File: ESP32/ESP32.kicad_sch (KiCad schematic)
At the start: 10 parts, among them U1 TPS63001

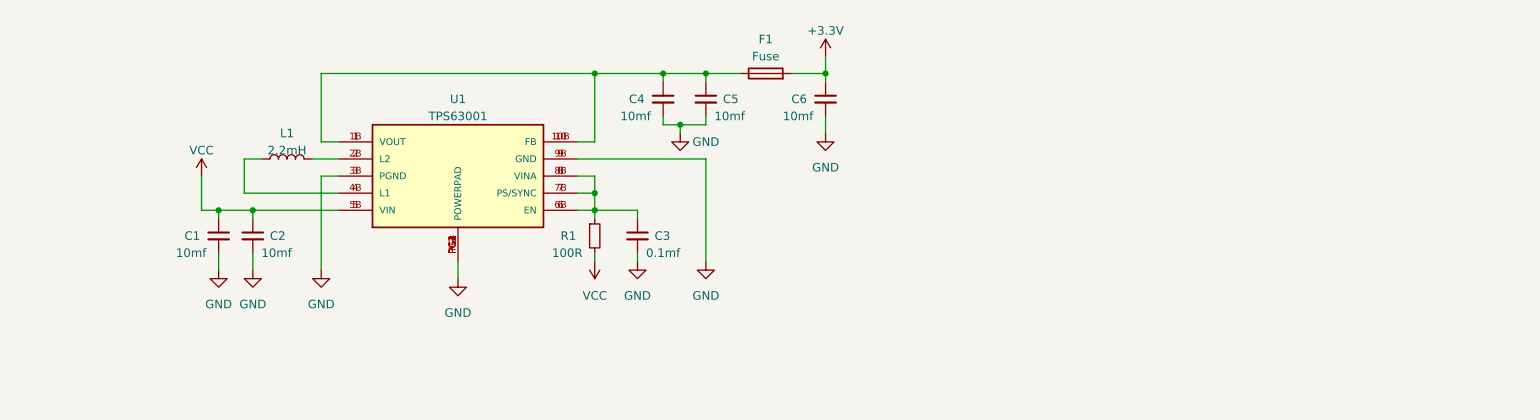
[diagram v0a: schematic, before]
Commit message: added power regulator and battery charger
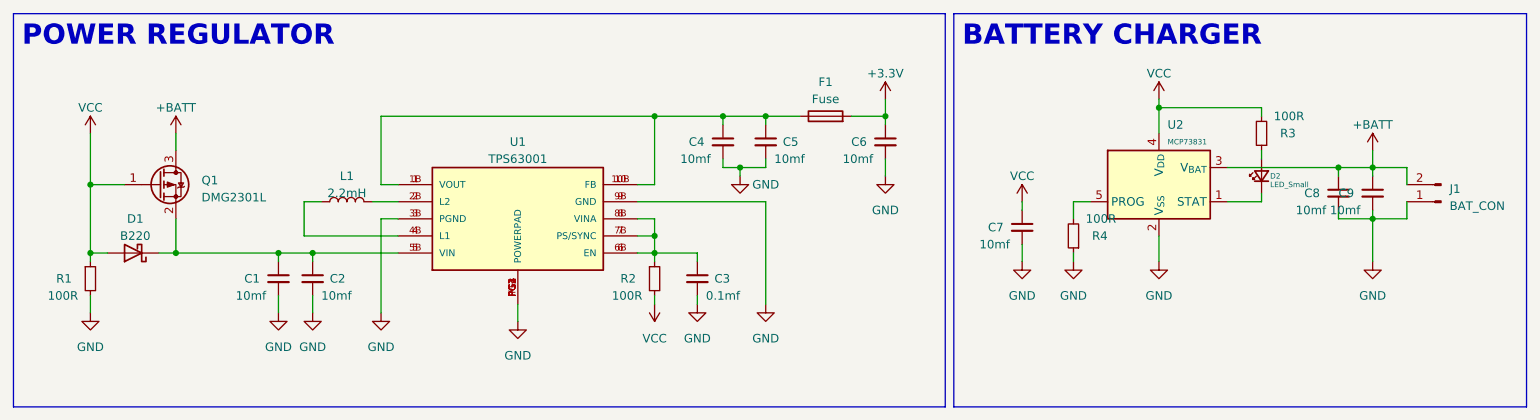
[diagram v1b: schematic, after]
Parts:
- added C7, C8, C9: 10mf, symbol Device:C_Small
- added D1: B220, Diode_SMD:D_SMB, symbol Diode:B220
- added D2: LED_Small, symbol Device:LED_Small
- added J1: BAT_CON, symbol Connector:Conn_01x02_Pin
- added Q1: DMG2301L, Package_TO_SOT_SMD:SOT-23, symbol Transistor_FET:DMG2301L
- added R1, R3, R4: 100R, symbol Device:R_Small
- added U2: MCP73831, Package_TO_SOT_SMD:SOT-23-5, symbol Battery_Management:MCP73831-4-OT
- renumbered R1 to R2
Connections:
- net GND: now also C7.2, C8.2, C9.2, J1.1 (Pin_1), R1.2, R4.1, U2.2 (V_{SS})
- net VCC: now also C7.1, D1.2 (A), Q1.1 (G), R1.1, R3.2, U2.4 (V_{DD}); no longer C1.1, C2.1, U1.5 (VIN), U1.5B (VIN)
- new net: C1.1, C2.1, D1.1 (K), Q1.2 (S), U1.5 (VIN), U1.5B (VIN)
- new net: D2.2 (A), R3.1
- new net: D2.1 (K), U2.1 (STAT)
- new net: R4.2, U2.5 (PROG)
- new net +BATT: C8.1, C9.1, J1.2 (Pin_2), Q1.3 (D), U2.3 (V_{BAT})
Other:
- note added: "BATTERY CHARGER"
- note added: "POWER REGULATOR"
- moved on the sheet: C1, C2, C3, C4, C5, C6, F1, L1, R2, U1

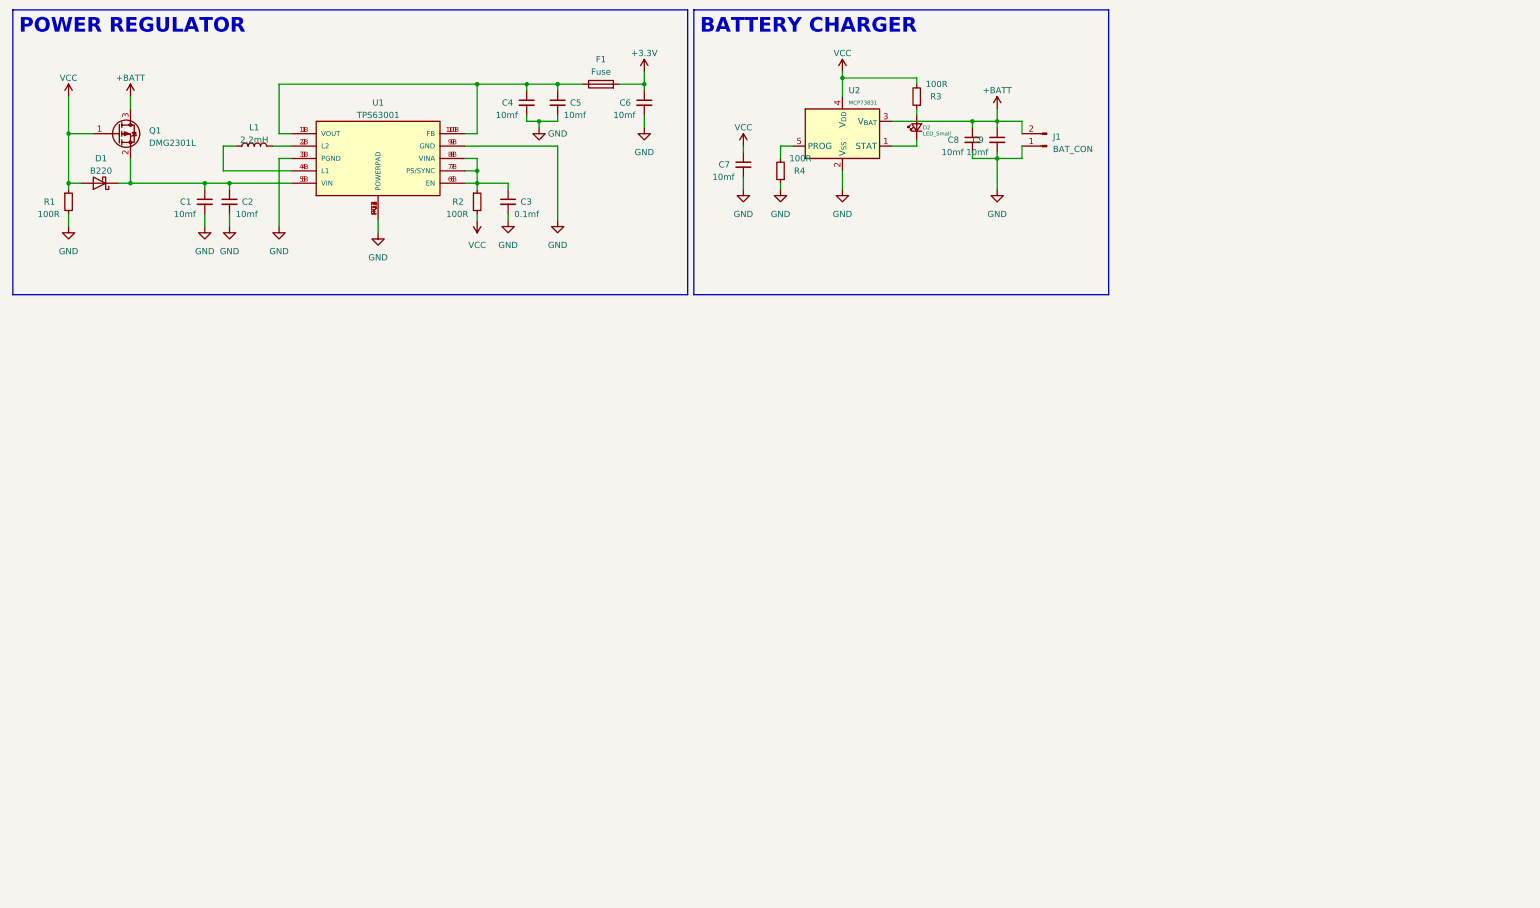
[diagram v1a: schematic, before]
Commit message: addes the memory chips
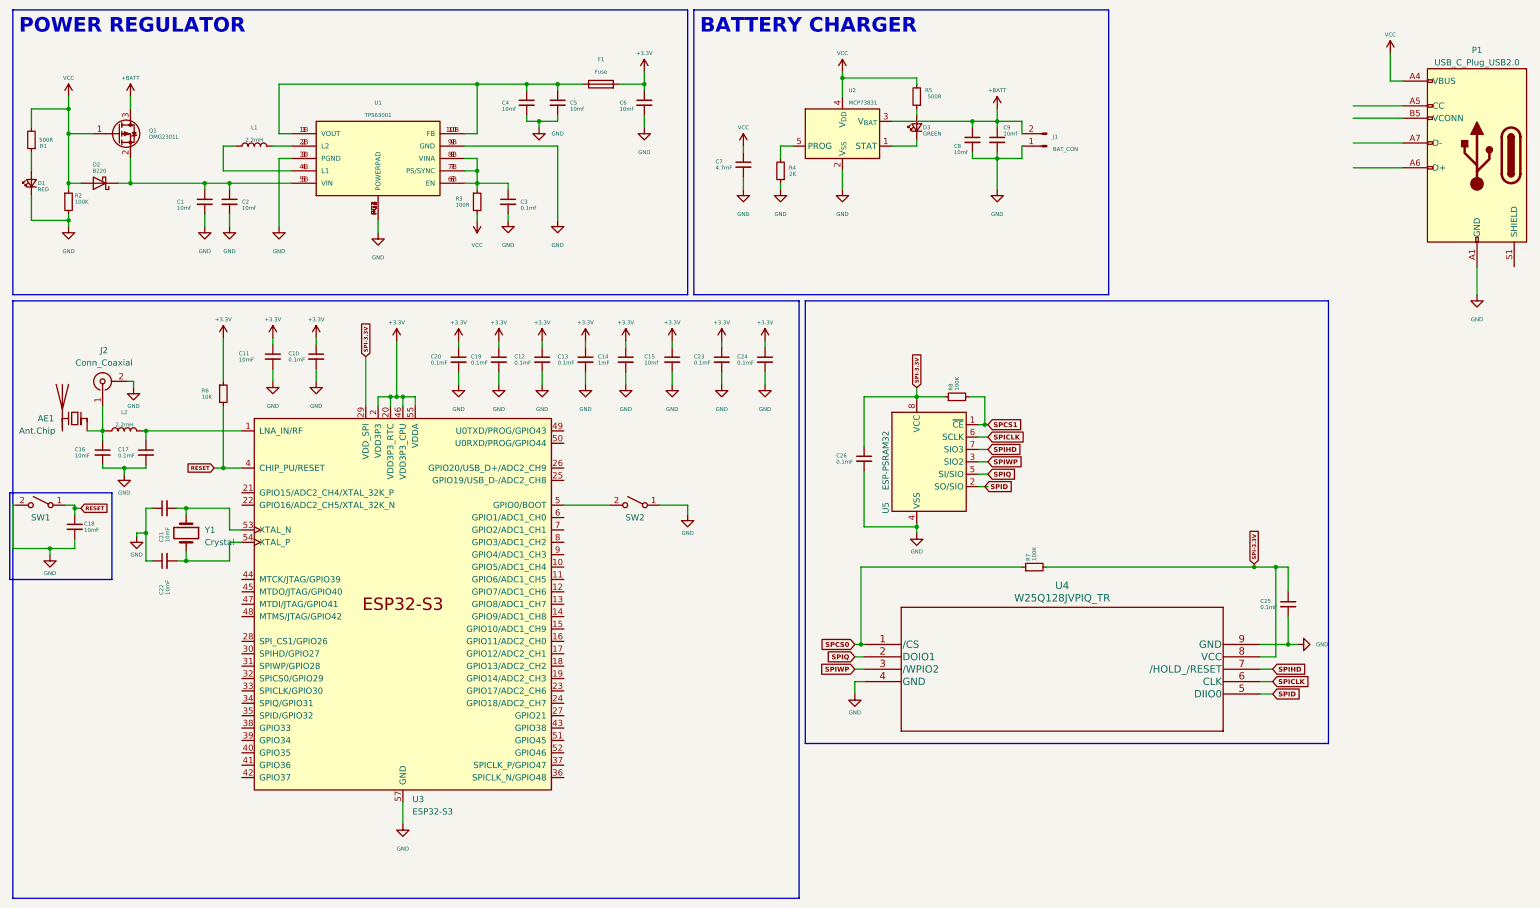
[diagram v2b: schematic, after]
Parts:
- added AE1: Ant.Chip, symbol Device:Antenna_Chip
- added C10, C12, C13, C17, C19, C20, C23, C24, C25, C26: 0.1mF, symbol Device:C_Small
- added C11, C16, C18, C21, C22: 10mF, symbol Device:C_Small
- added C14: 1mF, symbol Device:C_Small
- added C15: 10mf, symbol Device:C_Small
- added D1: RED, symbol Device:LED_Small
- added J2: Conn_Coaxial, symbol Connector:Conn_Coaxial
- added L2: 2.2mH, symbol Device:L
- added P1: USB_C_Plug_USB2.0, symbol Connector:USB_C_Plug_USB2.0
- added R1: 500R, symbol Device:R_Small
- added R6: 10K, symbol Device:R_Small
- added R7, R8: 100K, symbol Device:R_Small
- added SW1, SW2: SW_SPST, symbol Switch:SW_SPST
- added U3: ESP32-S3, Package_DFN_QFN:QFN-56-1EP_7x7mm_P0.4mm_EP5.6x5.6mm, symbol Espressif:ESP32-S3
- added U4: W25Q128JVPIQ_TR, WSON-8_6X5_WIN, symbol 2023-03-15_14-57-46:W25Q128JVPIQ_TR
- added U5: ESP-PSRAM32, Package_SO:SOIC-8_3.9x4.9mm_P1.27mm, symbol Memory_RAM:ESP-PSRAM32
- added Y1: Crystal, symbol Device:Crystal
- C7: value 10mf -> 4.7mF
- D3: renamed from D2; value LED_Small -> GREEN
- R2: renamed from R1; value 100R -> 100K
- R4: value 100R -> 2K
- R5: renamed from R3; value 100R -> 500R
- renumbered D1 to D2, R2 to R3
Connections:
- net +3.3V: now also C10.1, C11.1, C12.1, C13.1, C14.1, C15.1, C19.1, C20.1, C23.1, C24.1, R6.1, U3.2 (VDD3P3), U3.20 (VDD3P3_RTC), U3.3 (VDD3P3), U3.46 (VDD3P3_CPU), U3.55 (VDDA), U3.56 (VDDA)
- net GND: now also C10.2, C11.2, C12.2, C13.2, C14.2, C15.2, C16.2, C17.2, C18.2, C19.2, C20.2, C21.1, C22.1, C23.2, C24.2, C25.2, C26.2, D1.1 (K), J2.2 (Ext), P1.A1 (GND), P1.A12 (GND), P1.B1 (GND), P1.B12 (GND), SW1.2 (B), SW2.1 (A), U3.57 (GND), U4.4 (GND), U4.9 (GND), U5.4 (VSS)
- net VCC: now also P1.A4 (VBUS), P1.A9 (VBUS), P1.B4 (VBUS), P1.B9 (VBUS), R1.2
- new net: D1.2 (A), R1.1
- new net: C17.1, L2.2, U3.1 (LNA_IN/RF)
- new net: AE1.1 (FEED), C16.1, J2.1 (In), L2.1
- new net: SW2.2 (B), U3.5 (GPIO0/BOOT)
- new net: C21.2, U3.53 (XTAL_N), Y1.1
- new net: C22.2, U3.54 (XTAL_P), Y1.2
- new net RESET: C18.1, R6.2, SW1.1 (A), U3.4 (CHIP_PU/RESET)
- new net SPCS0: R7.1, U4.1 (/CS)
- new net SPCS1: R8.2, U5.1 (~{CE})
- new net SPI-3.3V: C25.1, C26.1, R7.2, R8.1, U3.29 (VDD_SPI), U4.8 (VCC), U5.8 (VCC)
- new net SPICLK: U4.6 (CLK), U5.6 (SCLK)
- new net SPID: U4.5 (DIIO0), U5.2 (SO/SIO)
- new net SPIHD: U4.7 (/HOLD_/RESET), U5.7 (SIO3)
- new net SPIQ: U4.2 (DOIO1), U5.5 (SI/SIO)
- new net SPIWP: U4.3 (/WPIO2), U5.3 (SIO2)

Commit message: Added Gpio and remaing cicuits
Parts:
- added C27: 4.7mF, symbol Device:C_Small
- added CR1: USBLC6-2SC6, SOT23-6L_STM, symbol USBLC6:USBLC6-2SC6
- added D4: WS2812B, LED_SMD:LED_WS2812B_PLCC4_5.0x5.0mm_P3.2mm, symbol LED:WS2812B
- added J3, J4: Conn_02x10_Odd_Even, symbol Connector_Generic:Conn_02x10_Odd_Even
- added JP1: Jumper_2_Open, symbol Jumper:Jumper_2_Open
- added R10, R11, R12, R9: 10K, symbol Device:R_Small
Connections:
- net +3.3V: now also J3.20 (Pin_20), J4.2 (Pin_2), JP1.2 (B)
- net +BATT: now also J4.17 (Pin_17), J4.19 (Pin_19), R11.1
- net GND: now also C27.2, CR1.2 (GND), D4.3 (VSS), J3.19 (Pin_19), J4.1 (Pin_1), J4.15 (Pin_15), R10.2, R12.2
- net RESET: now also J4.9 (Pin_9)
- net SPID: now also U3.35 (SPID/GPIO32)
- net SPIHD: now also U3.30 (SPIHD/GPIO27)
- net SPIQ: now also U3.34 (SPIQ/GPIO31)
- net SPIWP: now also U3.31 (SPIWP/GPIO28)
- net VCC: now also C1.1, C2.1, D2.1 (K), Q1.2 (S), U1.5 (VIN), U1.5B (VIN), J4.11 (Pin_11), J4.13 (Pin_13); no longer D2.2 (A), Q1.1 (G), R1.2, R2.1, R5.2, U2.4 (V_{DD})
- net at P1.A6 (D+): now also CR1.3 (I/O2)
- net at P1.A7 (D-): now also CR1.1 (I/O1)
- net IO5: now reaches U3.10 (GPIO5/ADC1_CH4)
- net IO5: now also J3.9 (Pin_9)
- net IO6: now reaches U3.11 (GPIO6/ADC1_CH5)
- net IO6: now also J3.11 (Pin_11)
- net IO7: now reaches U3.12 (GPIO7/ADC1_CH6)
- net IO7: now also J3.13 (Pin_13)
- net IO8: now reaches U3.13 (GPIO8/ADC1_CH7)
- net IO8: now also J3.15 (Pin_15)
- net IO9: now reaches U3.14 (GPIO9/ADC1_CH8)
- net IO9: now also J3.17 (Pin_17)
- net IO10: now reaches U3.15 (GPIO10/ADC1_CH9)
- net IO10: now also J4.3 (Pin_3)
- net USB-VOLT: now reaches U3.16 (GPIO11/ADC2_CH0)
- net USB-VOLT: now also R10.1, R9.2
- net BAT-VOLT: now reaches U3.17 (GPIO12/ADC2_CH1)
- net BAT-VOLT: now also R11.2, R12.1
- net IO13: now reaches U3.18 (GPIO13/ADC2_CH2)
- net IO13: now also J3.2 (Pin_2)
- net IO14: now reaches U3.19 (GPIO14/ADC2_CH3)
- net IO14: now also J3.4 (Pin_4)
- net GPIO15: now reaches U3.21 (GPIO15/ADC2_CH4/XTAL_32K_P)
- net GPIO16: now reaches U3.22 (GPIO16/ADC2_CH5/XTAL_32K_N)
- net IO17: now reaches U3.23 (GPIO17/ADC2_CH6)
- net IO17: now also J3.10 (Pin_10)
- net IO18: now reaches U3.24 (GPIO18/ADC2_CH7)
- net IO18: now also J3.12 (Pin_12)
- net IO21: now reaches U3.27 (GPIO21)
- net IO21: now also J3.14 (Pin_14)
- net SPICS1: now reaches U3.28 (SPI_CS1/GPIO26)
- net SPICS0: now reaches U3.32 (SPICS0/GPIO29)
- net SPCLK: now reaches U3.33 (SPICLK/GPIO30)
- net IO48: now reaches U3.36 (SPICLK_N/GPIO48)
- net IO47: now reaches U3.37 (SPICLK_P/GPIO47)
- net IO33: now reaches U3.38 (GPIO33)
- net IO33: now also J3.16 (Pin_16)
- net IO34: now reaches U3.39 (GPIO34)
- net IO34: now also J3.18 (Pin_18)
- net IO35: now reaches U3.40 (GPIO35)
- net IO35: now also J4.4 (Pin_4)
- net IO36: now reaches U3.41 (GPIO36)
- net IO36: now also J4.6 (Pin_6)
- net IO37: now reaches U3.42 (GPIO37)
- net IO37: now also J4.8 (Pin_8)
- net IO38: now reaches U3.43 (GPIO38)
- net IO38: now also J4.10 (Pin_10)
- net GPIO39: now reaches U3.44 (MTCK/JTAG/GPIO39)
- net GPIO40: now reaches U3.45 (MTDO/JTAG/GPIO40)
- net GPIO41: now reaches U3.47 (MTDI/JTAG/GPIO41)
- net GPIO42: now reaches U3.48 (MTMS/JTAG/GPIO42)
- net TX/0: now reaches U3.49 (U0TXD/PROG/GPIO43)
- net TX/0: now also J4.5 (Pin_5)
- net RX/0: now reaches U3.50 (U0RXD/PROG/GPIO44)
- net RX/0: now also J4.7 (Pin_7)
- net IO45: now reaches U3.51 (GPIO45)
- net IO45: now also D4.4 (DIN)
- net IO46: now reaches U3.52 (GPIO46)
- net IO1: now reaches U3.6 (GPIO1/ADC1_CH0)
- net IO1: now also J3.1 (Pin_1)
- net IO2: now reaches U3.7 (GPIO2/ADC1_CH1)
- net IO2: now also J3.3 (Pin_3)
- net IO3: now reaches U3.8 (GPIO3/ADC1_CH2)
- net IO3: now also J3.5 (Pin_5)
- net IO4: now reaches U3.9 (GPIO4/ADC1_CH3)
- net IO4: now also J3.7 (Pin_7)
- new net: D4.1 (VDD), JP1.1 (A)
- new net D+: CR1.4 (I/O2)
- new net D-: CR1.6 (I/O1)
- new net IO15: J3.6 (Pin_6)
- new net IO16: J3.8 (Pin_8)
- new net IO39: J4.12 (Pin_12)
- new net IO40: J4.14 (Pin_14)
- new net IO41: J4.16 (Pin_16)
- new net IO42: J4.18 (Pin_18)
- new net VBUS: C27.1, CR1.5 (VBUS), D2.2 (A), J4.20 (Pin_20), Q1.1 (G), R1.2, R2.1, R5.2, R9.1, U2.4 (V_{DD})
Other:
- note added: "GPIO D&A"
- note added: "GPIO/DIGITAL & ANALOG"
- note added: "I2C"
- note added: "JTAG"
- note added: "RX/TX"
- moved on the sheet: C18, C21, C22, P1, SW1, Y1

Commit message: added notes
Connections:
- net at C21.2, Y1.1: no longer U3.53 (XTAL_N)
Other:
- note added: "GPIO"
- note added: "IMPORTANT NOTES RELATED TO DESIGN"
- note added: "INTERNAL FEATURES"
- note added: "MEMORY"
- note added: "MICROCONTROLLER"
- note added: "USB C"
- moved on the sheet: C25, C26, D4, J3, J4, JP1, R10, R11, R12, R6, R7, R8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

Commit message: added footprints
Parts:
- removed AE1: Ant.Chip, symbol Device:Antenna_Chip
- added AE1: Chip Ant., Johanson:2450AT42A100E, symbol Johanson Antenna:2450AT42A100E
- added R13, R14: 5.1K, Resistor_SMD:R_0402_1005Metric, symbol Device:R_Small
- C1, C2, C3, C4, C5, C6, C8, C9: footprint (none) -> Capacitor_SMD:C_0805_2012Metric
- C10, C11, C12, C13, C14, C15, C16, C17, C18, C19, C20, C21, C22, C23, C24, C25, C26, C27: footprint (none) -> Capacitor_SMD:C_0402_1005Metric
- C7: footprint (none) -> Capacitor_SMD:C_0603_1608Metric
- CR1: footprint SOT23-6L_STM -> ESD:USBLC6-2SC6
- D1, D3: footprint (none) -> LED_SMD:LED_0603_1608Metric
- D4: footprint LED_SMD:LED_WS2812B_PLCC4_5.0x5.0mm_P3.2mm -> LED_SMD:LED_WS2812B-2020_PLCC4_2.0x2.0mm
- F1: footprint (none) -> Fuse:Fuse_0805_2012Metric_Pad1.15x1.40mm_HandSolder
- J1: footprint (none) -> Connector_JST:JST_SHL_SM02B-SHLS-TF_1x02-1MP_P1.00mm_Horizontal
- J2: footprint (none) -> Connector_Coaxial:U.FL_Molex_MCRF_73412-0110_Vertical
- J3, J4: footprint (none) -> footprints:BM28B0.6-20DS&slash_2-0.35V51
- JP1: footprint (none) -> Jumper:SolderJumper-2_P1.3mm_Open_TrianglePad1.0x1.5mm
- L1: footprint (none) -> Inductor_SMD:L_0402_1005Metric
- L2: footprint (none) -> Inductor_SMD:L_0603_1608Metric
- P1: footprint (none) -> USB-C:MOLEX_2169900003
- R1, R10, R11, R12, R2, R3, R4, R5, R6, R7, R8, R9: footprint (none) -> Resistor_SMD:R_0402_1005Metric
- SW1, SW2: footprint (none) -> Button:SW_SKRPACE010
- U1: footprint TPS63001 -> TPS63001:TPS63001
- U4: footprint WSON-8_6X5_WIN -> Winbond:SON127P610X510X80-8N430X340
- Y1: footprint (none) -> Crystal:Crystal_SMD_0603-4Pin_6.0x3.5mm
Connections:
- net D+: now also U3.26 (GPIO20/USB_D+/ADC2_CH9)
- net D-: now also U3.25 (GPIO19/USB_D-/ADC2_CH8)
- net GND: now also R13.2, R14.2
- net VBUS: now also C7.1
- net VCC: no longer C7.1
- net at P1.A5 (CC): now also R14.1
- net at P1.B5 (VCONN): now also R13.1
- net at C16.1, J2.1 (In), L2.1: now also AE1.1
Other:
- moved on the sheet: C27, CR1

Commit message: Components are organized
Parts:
- removed C6: 10mf, Capacitor_SMD:C_0805_2012Metric, symbol Device:C_Small
- removed F1: Fuse, Fuse:Fuse_0805_2012Metric_Pad1.15x1.40mm_HandSolder, symbol Device:Fuse
- added D5: B220, Diode_SMD:D_SOD-323, symbol Diode:B220
- added F2: Fuse, Fuse:Fuse_0805_2012Metric_Pad1.15x1.40mm_HandSolder, symbol Device:Fuse
- AE1: footprint Johanson:2450AT42A100E -> Antenna:2450AT42A100E
- C1, C2, C4, C5: footprint Capacitor_SMD:C_0805_2012Metric -> Capacitor_SMD:C_0603_1608Metric
- C15: value 10mf -> 1mF
- C3: footprint Capacitor_SMD:C_0805_2012Metric -> Capacitor_SMD:C_0402_1005Metric
- D2: footprint Diode_SMD:D_SMB -> Diode_SMD:D_SOD-323
- J3, J4: footprint footprints:BM28B0.6-20DS&slash_2-0.35V51 -> FPC3:HRS_DF12NB-20DS-0.5V(51)
- R10: value 10K -> 2K
- R11: value 10K -> 442K
- R12: value 10K -> 160K
- R9: value 10K -> 3.3K
- Y1: footprint Crystal:Crystal_SMD_0603-4Pin_6.0x3.5mm -> Crystal:Crystal_SMD_3225-4Pin_3.2x2.5mm
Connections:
- net +3.3V: now also C4.1, C5.1, U1.1 (VOUT), U1.10 (FB), U1.10B (FB), U1.1B (VOUT)
- net VCC: now also D5.2 (A); no longer C1.1, C2.1, D2.1 (K), Q1.2 (S), U1.5 (VIN), U1.5B (VIN)
- new net: D2.1 (K), D5.1 (K), F2.1
- new net: C1.1, C2.1, F2.2, Q1.2 (S), U1.5 (VIN), U1.5B (VIN)
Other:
- moved on the sheet: Q1
